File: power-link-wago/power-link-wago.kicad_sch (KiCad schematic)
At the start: 12 parts, among them J101 NE8FAV, J102 NE8FAV, J103 WAGO 2601-1101, J104 WAGO 2601-1101, J105 WAGO 2601-1101, J106 WAGO 2601-1101

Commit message: Rename power-poe -> power-link-wago
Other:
- title: V2 Power PoE -> V2 Power Link WAGO
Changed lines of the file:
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@@
 	(paper "A4")
 	(title_block
-		(title "V2 Power PoE")
+		(title "V2 Power Link WAGO")
 		(date "2026-01-12")
 		(rev "3")
@@
 		)
 		(instances
-			(project "power-poe"
+			(project "power-link-wago"
 				(path "/6c8448b4-b04d-47e1-934e-e40cbe27a7be"
 					(reference "#FLG0103")
@@
 		)
 		(instances
-			(project "power-poe"
+			(project "power-link-wago"
 				(path "/6c8448b4-b04d-47e1-934e-e40cbe27a7be"
 					(reference "J103")
@@
 		)
 		(instances
-			(project "power-poe"
+			(project "power-link-wago"
 				(path "/6c8448b4-b04d-47e1-934e-e40cbe27a7be"
 					(reference "ICON103")
@@
 		)
 		(instances
-			(project "power-poe"
+			(project "power-link-wago"
 				(path "/6c8448b4-b04d-47e1-934e-e40cbe27a7be"
 					(reference "J106")
@@
 		)
 		(instances
-			(project "power-poe"
+			(project "power-link-wago"
 				(path "/6c8448b4-b04d-47e1-934e-e40cbe27a7be"
 					(reference "#PWR0108")
@@
 		)
 		(instances
-			(project "power-poe"
+			(project "power-link-wago"
 				(path "/6c8448b4-b04d-47e1-934e-e40cbe27a7be"
 					(reference "#PWR0107")
@@
 		)
 		(instances
-			(project "power-poe"
+			(project "power-link-wago"
 				(path "/6c8448b4-b04d-47e1-934e-e40cbe27a7be"
 					(reference "#PWR0110")
@@
 		)
 		(instances
-			(project "power-poe"
+			(project "power-link-wago"
 				(path "/6c8448b4-b04d-47e1-934e-e40cbe27a7be"
 					(reference "J105")
@@
 		)
 		(instances
-			(project "power-poe"
+			(project "power-link-wago"
 				(path "/6c8448b4-b04d-47e1-934e-e40cbe27a7be"
 					(reference "#PWR0111")
@@
 		)
 		(instances
-			(project "power-poe"
+			(project "power-link-wago"
 				(path "/6c8448b4-b04d-47e1-934e-e40cbe27a7be"
 					(reference "H102")

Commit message: Fix WAGOs
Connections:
- net +24V renamed +VLINK
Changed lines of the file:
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@@
 			)
 		)
-		(property "Description" "Power symbol creates a global label with name \"Earth\""
+		(property "Description" "Power symbol creates a global label with name \"Shield\""
 			(at 119.38 103.632 0)
 			(effects
@@
 	(symbol
 		(lib_id "V2_power:PWR_FLAG")
-		(at 149.86 55.88 90)
+		(at 149.86 54.61 90)
 		(unit 1)
 		(exclude_from_sim no)
@@
 		(dnp no)
 		(property "Reference" "#FLG0103"
-			(at 147.955 55.88 0)
+			(at 147.955 54.61 0)
 			(effects
 				(font
@@
 		)
 		(property "Value" "PWR_FLAG"
-			(at 138.938 55.88 90)
+			(at 138.938 54.61 90)
 			(effects
 				(font
@@
 		)
 		(property "Footprint" ""
-			(at 149.86 55.88 0)
-			(effects
-				(font
-					(size 1.27 1.27)
-				)
-				(hide yes)
-			)
-		)
-		(property "Datasheet" ""
-			(at 149.86 55.88 0)
+			(at 149.86 54.61 0)
+			(effects
+				(font
+					(size 1.27 1.27)
+				)
+				(hide yes)
+			)
+		)
+		(property "Datasheet" ""
+			(at 149.86 54.61 0)
 			(effects
 				(font
@@
 		)
 		(property "Description" "Special symbol for telling ERC where power comes from"
-			(at 167.132 55.88 0)
+			(at 167.132 54.61 0)
 			(effects
 				(font
@@
 	)
 	(symbol
-		(lib_id "V2_power:+24V")
+		(lib_id "V2_power:+VLINK")
 		(at 149.86 44.45 270)
 		(unit 1)
@@
 			)
 		)
-		(property "Value" "+24V"
+		(property "Value" "+VLINK"
 			(at 156.972 44.45 90)
 			(effects
@@
 			)
 		)
-		(property "Description" "Power symbol creates a global label with name \"+24V\""
+		(property "Description" "Power symbol creates a global label with name \"+VLINK\""
 			(at 135.128 44.45 0)
 			(effects
@@
 	)
 	(symbol
-		(lib_id "V2_power:+24V")
+		(lib_id "V2_power:+VLINK")
 		(at 158.75 135.89 0)
 		(unit 1)
@@
 			)
 		)
-		(property "Value" "+24V"
+		(property "Value" "+VLINK"
 			(at 156.464 130.81 0)
 			(effects
@@
 			)
 		)
-		(property "Description" "Power symbol creates a global label with name \"+24V\""
+		(property "Description" "Power symbol creates a global label with name \"+VLINK\""
 			(at 158.75 150.622 0)
 			(effects
@@
 			)
 		)
-		(property "Description" "Power symbol creates a global label with name \"Earth\""
+		(property "Description" "Power symbol creates a global label with name \"Shield\""
 			(at 165.1 103.632 0)
 			(effects
@@
 	)
 	(symbol
-		(lib_id "V2_power:+24V")
+		(lib_id "V2_power:+VLINK")
 		(at 129.54 77.47 270)
 		(unit 1)
@@
 			)
 		)
-		(property "Value" "+24V"
+		(property "Value" "+VLINK"
 			(at 133.35 77.4699 90)
 			(effects
@@
 			)
 		)
-		(property "Description" "Power symbol creates a global label with name \"+24V\""
+		(property "Description" "Power symbol creates a global label with name \"+VLINK\""
 			(at 114.808 77.47 0)
 			(effects
@@
 	)
 	(symbol
-		(lib_id "V2_power:+24V")
+		(lib_id "V2_power:+VLINK")
 		(at 175.26 77.47 270)
 		(unit 1)
@@
 			)
 		)
-		(property "Value" "+24V"
+		(property "Value" "+VLINK"
 			(at 179.07 77.4699 90)
 			(effects
@@
 			)
 		)
-		(property "Description" "Power symbol creates a global label with name \"+24V\""
+		(property "Description" "Power symbol creates a global label with name \"+VLINK\""
 			(at 160.528 77.47 0)
 			(effects
@@
 	(symbol
 		(lib_id "V2_power:Shield")
-		(at 149.86 55.88 90)
+		(at 149.86 54.61 90)
 		(unit 1)
 		(exclude_from_sim no)
@@
 		(fields_autoplaced yes)
 		(property "Reference" "#PWR0111"
-			(at 157.48 55.88 0)
+			(at 157.48 54.61 0)
 			(effects
 				(font
@@
 		)
 		(property "Value" "Shield"
-			(at 153.67 55.8799 90)
+			(at 153.67 54.6099 90)
 			(effects
 				(font
@@
 		)
 		(property "Footprint" ""
-			(at 149.86 55.88 0)
-			(effects
-				(font
-					(size 1.27 1.27)
-				)
-				(hide yes)
-			)
-		)
-		(property "Datasheet" ""
-			(at 149.86 55.88 0)
-			(effects
-				(font
-					(size 1.27 1.27)
-				)
-				(hide yes)
-			)
-		)
-		(property "Description" "Power symbol creates a global label with name \"Earth\""
-			(at 160.782 55.88 0)
-			(effects
-				(font
+			(at 149.86 54.61 0)
+			(effects
+				(font
+					(size 1.27 1.27)
+				)
+				(hide yes)
+			)
+		)
+		(property "Datasheet" ""
+			(at 149.86 54.61 0)
+			(effects
+				(font
+					(size 1.27 1.27)
+				)
+				(hide yes)
+			)
+		)
+		(property "Description" "Power symbol creates a global label with name \"Shield\""
+			(at 160.782 54.61 0)
+			(effects
+				(font

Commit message: Use date as revision
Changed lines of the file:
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@@
 	(title_block
 		(title "V2 Power Link WAGO")
-		(date "2026-01-12")
-		(rev "3")
+		(date "2026-02-10")
+		(rev "2026-01-12")
 		(company "Versio Duo")
 	)
@@
 			)
 		)
-		(property "Description" "Power symbol creates a global label with name \"Shield\""
+		(property "Description" ""
 			(at 119.38 103.632 0)
 			(effects
@@
 			)
 		)
-		(property "Description" "Power symbol creates a global label with name \"GND\" , ground"
+		(property "Description" ""
 			(at 160.274 49.784 0)
 			(effects
@@
 			)
 		)
-		(property "Description" "Power symbol creates a global label with name \"+VLINK\""
+		(property "Description" "Power Over CAT Cable"
 			(at 135.128 44.45 0)
 			(effects
@@
 			)
 		)
-		(property "Description" "Power symbol creates a global label with name \"GND\" , ground"
+		(property "Description" ""
 			(at 122.936 153.924 0)
 			(effects
@@
 			)
 		)
-		(property "Description" "Power symbol creates a global label with name \"+VLINK\""
+		(property "Description" "Power Over CAT Cable"
 			(at 158.75 150.622 0)
 			(effects
@@
 			)
 		)
-		(property "Description" "Power symbol creates a global label with name \"Shield\""
+		(property "Description" ""
 			(at 165.1 103.632 0)
 			(effects
@@
 			)
 		)
-		(property "Description" "Power symbol creates a global label with name \"+VLINK\""
+		(property "Description" "Power Over CAT Cable"
 			(at 114.808 77.47 0)
 			(effects
@@
 			)
 		)
-		(property "Description" "Power symbol creates a global label with name \"GND\" , ground"
+		(property "Description" ""
 			(at 185.674 70.104 0)
 			(effects
@@
 			)
 		)
-		(property "Description" "Power symbol creates a global label with name \"GND\" , ground"
+		(property "Description" ""
 			(at 139.954 70.104 0)
 			(effects
@@
 			)
 		)
-		(property "Description" "Power symbol creates a global label with name \"+VLINK\""
+		(property "Description" "Power Over CAT Cable"
 			(at 160.528 77.47 0)
 			(effects
@@
 			)
 		)
-		(property "Description" "Power symbol creates a global label with name \"Shield\""
+		(property "Description" ""
 			(at 160.782 54.61 0)
 			(effects
@@
 	)
 	(embedded_fonts no)
+	(embedded_files
+		(file
+			(name "V2_A4.kicad_wks")
+			(type worksheet)
+			(data |KLUv/WBhBk0QALbYTiEQtRsmZc5q276ayLS71D6kxbkmoTeIJM7lAHtEAMAAxQFGAD8ARQCbvIHa
+				a/wrVHSazXnPhvzar1BNtH1kxRf5EwCAQPh5F+e0kJq0nmtfKDvj37Jf3xQUlFKqztoXWzE7iAAI
+				iJ6Q5m2d9RAC9jcPPWe/GXf/9ewpPR3+uPbv7bdzvr37wXlr2X8dBHFXu7Z3HUG7Kvrz9qKU7eB2
+				v/MM4n/Mhfg5G5sn7WsDTS2mA1WyssZDsy4YdpEGzfD8Ny+85JzH7H+961FjX/x0qtq0MdaqJ8dx
+				k1KAwF+soV3VFnEoqewX+XNfTaqqPatRlLsbgcKhzs5+29sEzSaWRPZ4txDEjpmZNCoSiiMhaUwy
+				y4Jg3oe5pmhPRSS7MtJAerbfnYNNgaEkuCg6oVzYhbEsF1vRgtxS55zTIVig4URjFFJTI1qYFNIB
+				YESmRusYYvaiF0uSUdhu1Q2lFiOgdmN7VvaH2oWyw9MQXRuZtQQQoIsxFn2ldtnpQiUNa0HvDQCK
+				f/XTisCgEJQEXe/if4EJsakkqj8BMmGAU+ZM/AG8LSEJMfgkOKfSKPhw4rD3ZHfmNZYNfDMigEPJ
+				EBoIDghtm1kJ8BAQ8xyGdkOuFQy33sishFt8DZNX4uNRXJZ5hBy746RJaNtgbfyB613d0dov6Cdg
+				iUQT9BXkf9EiYDuODpB6gKkC|
+			)
+			(checksum "0A61268C685EAF945CA2EA8187370BD3")
+		)
+	)
 )

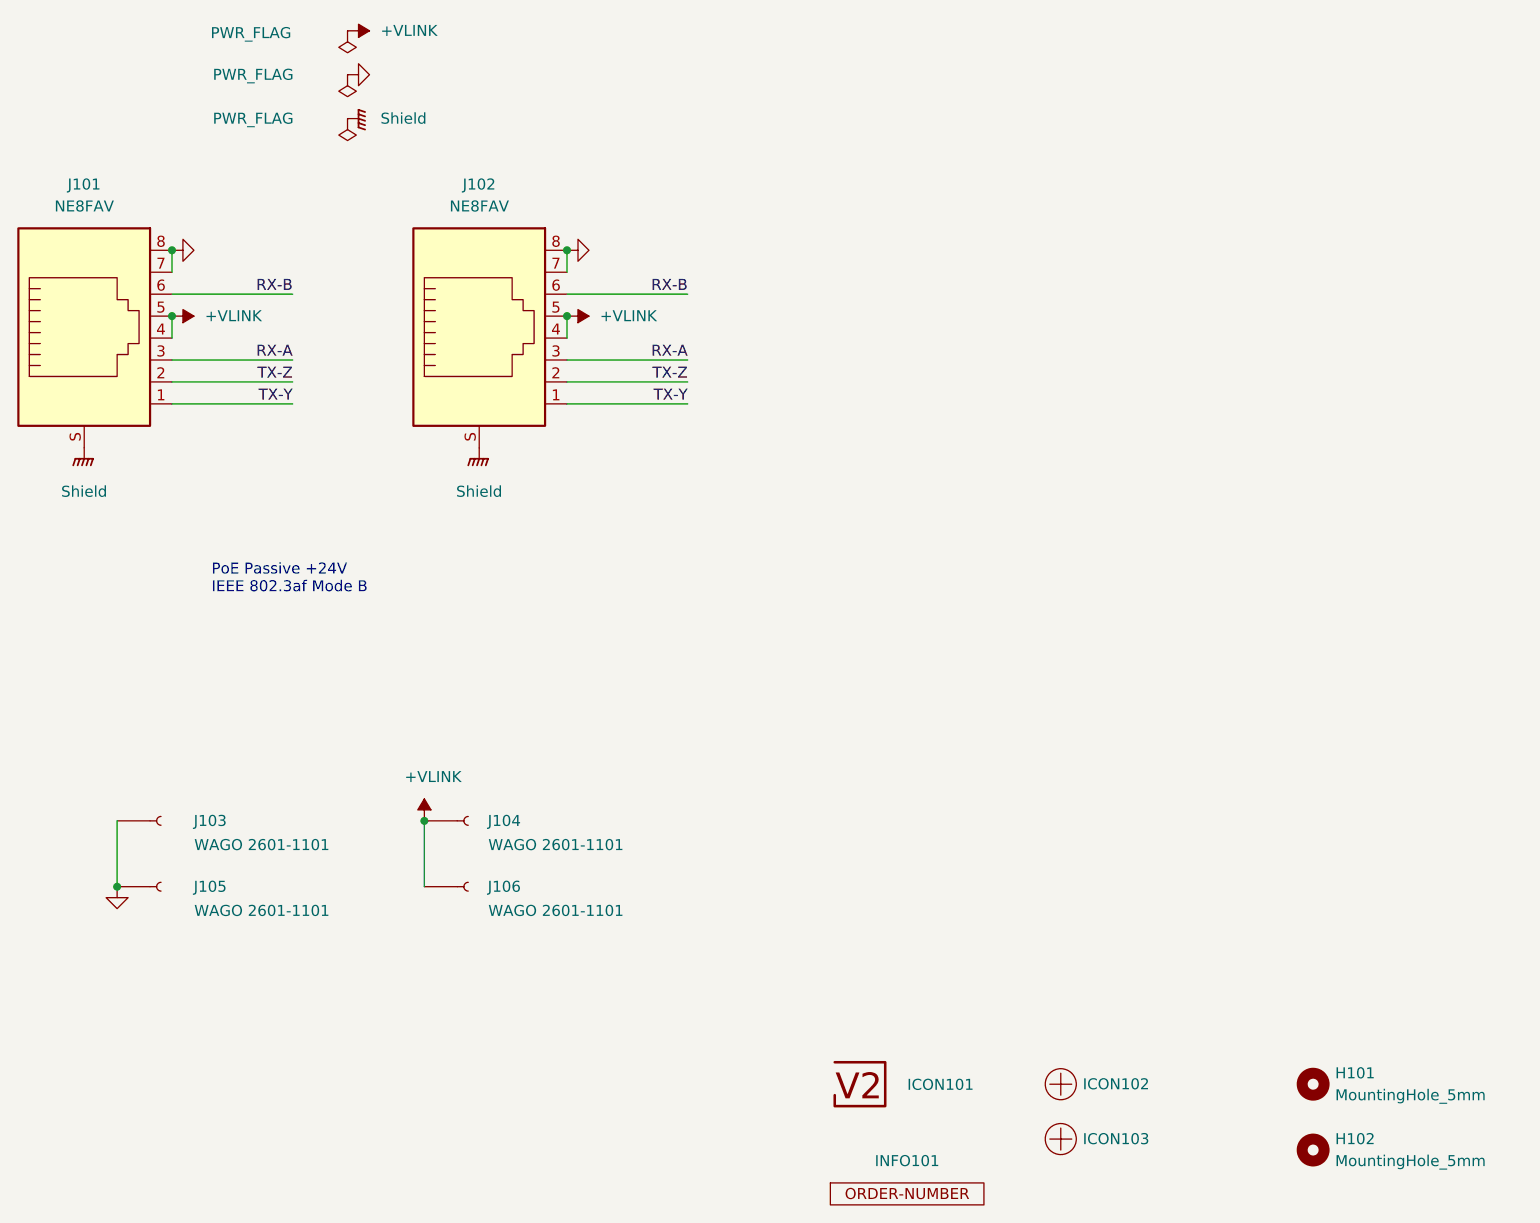
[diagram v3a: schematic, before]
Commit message: Replace Order_Number
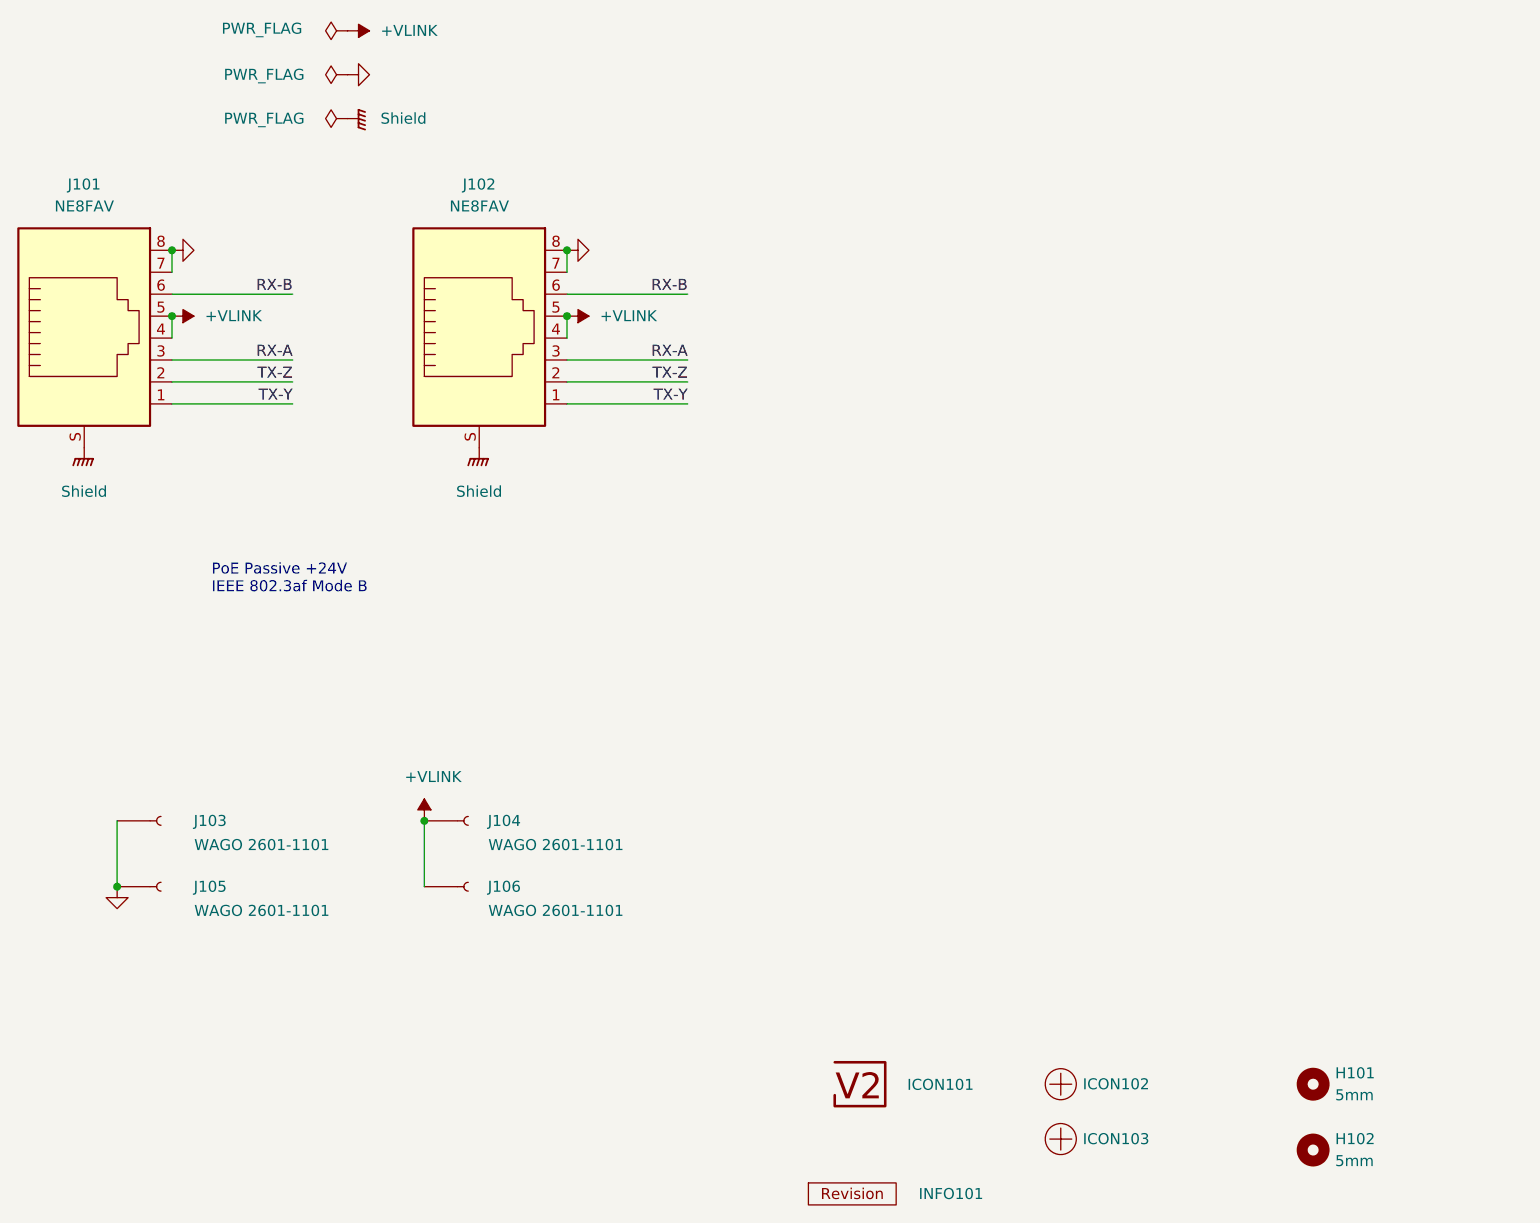
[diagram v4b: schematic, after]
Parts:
- H101, H102: value MountingHole_5mm -> 5mm
- INFO101: value Order_Number -> ~; footprint V2_Production:Order_Number -> V2_Production:Revision; symbol V2_Production:Order_Number -> V2_Production:Revision
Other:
- moved on the sheet: INFO101
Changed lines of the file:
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@@
 	(symbol
 		(lib_id "V2_power:PWR_FLAG")
-		(at 149.86 54.61 90)
+		(at 149.86 54.61 0)
 		(unit 1)
 		(exclude_from_sim no)
@@
 		(dnp no)
 		(property "Reference" "#FLG0103"
-			(at 147.955 54.61 0)
+			(at 149.86 52.705 0)
 			(effects
 				(font
@@
 		)
 		(property "Value" "PWR_FLAG"
-			(at 138.938 54.61 90)
+			(at 140.208 54.61 0)
 			(effects
 				(font
@@
 		)
 		(property "Description" "Special symbol for telling ERC where power comes from"
-			(at 167.132 54.61 0)
+			(at 149.86 71.882 0)
 			(effects
 				(font
@@
 			)
 		)
-		(property "Sim.Enable" "0"
-			(at 209.55 166.37 0)
-			(effects
-				(font
-					(size 1.27 1.27)
-				)
-				(hide yes)
-			)
-		)
 		(instances
 			(project ""
@@
 	(symbol
 		(lib_id "V2_power:PWR_FLAG")
-		(at 149.86 49.53 90)
+		(at 149.86 49.53 0)
 		(unit 1)
 		(exclude_from_sim no)
@@
 		(dnp no)
 		(property "Reference" "#FLG0102"
-			(at 147.955 49.53 0)
+			(at 149.86 47.625 0)
 			(effects
 				(font
@@
 		)
 		(property "Value" "PWR_FLAG"
-			(at 138.938 49.53 90)
+			(at 140.208 49.53 0)
 			(effects
 				(font
@@
 		)
 		(property "Description" "Special symbol for telling ERC where power comes from"
-			(at 167.132 49.53 0)
+			(at 149.86 66.802 0)
 			(effects
 				(font
@@
 	)
 	(symbol
-		(lib_id "V2_Production:Order_Number")
-		(at 214.63 179.07 0)
+		(lib_id "V2_Production:Revision")
+		(at 208.28 179.07 0)
 		(unit 1)
 		(exclude_from_sim no)
@@
 		(dnp no)
 		(property "Reference" "INFO101"
-			(at 214.63 175.26 0)
-			(effects
-				(font
-					(size 1.27 1.27)
-				)
-			)
-		)
-		(property "Value" "Order_Number"
-			(at 214.63 181.61 0)
-			(effects
-				(font
-					(size 1.27 1.27)
-				)
-				(hide yes)
-			)
-		)
-		(property "Footprint" "V2_Production:Order_Number"
-			(at 214.63 184.15 0)
-			(effects
-				(font
-					(size 1.27 1.27)
-				)
-				(hide yes)
-			)
-		)
-		(property "Datasheet" ""
-			(at 214.63 179.07 0)
+			(at 219.71 179.07 0)
+			(effects
+				(font
+					(size 1.27 1.27)
+				)
+			)
+		)
+		(property "Value" "~"
+			(at 208.28 181.61 0)
+			(effects
+				(font
+					(size 1.27 1.27)
+				)
+				(hide yes)
+			)
+		)
+		(property "Footprint" "V2_Production:Revision"
+			(at 208.28 184.15 0)
+			(effects
+				(font
+					(size 1.27 1.27)
+				)
+				(hide yes)
+			)
+		)
+		(property "Datasheet" ""
+			(at 208.28 179.07 0)
 			(effects
 				(font
@@
 		)
 		(property "Description" ""
-			(at 214.63 179.07 0)
+			(at 208.28 179.07 0)
 			(effects
 				(font
@@
 			)
 		)
-		(property "Value" "MountingHole_5mm"
+		(property "Value" "5mm"
 			(at 264.16 167.6399 0)
 			(effects
@@
 			)
 		)
-		(property "Sim.Enable" "0"
-			(at 261.62 166.37 0)
-			(effects
-				(font
-					(size 1.27 1.27)
-				)
-				(hide yes)
-			)
-		)
 		(instances
 			(project ""
@@
 	(symbol
 		(lib_id "V2_power:PWR_FLAG")
-		(at 149.86 44.45 90)
+		(at 149.86 44.45 0)
 		(unit 1)
 		(exclude_from_sim no)
@@
 		(dnp no)
 		(property "Reference" "#FLG0101"
-			(at 147.955 44.45 0)
+			(at 149.86 42.545 0)
 			(effects
 				(font
@@
 		)
 		(property "Value" "PWR_FLAG"
-			(at 138.684 44.704 90)
+			(at 139.954 44.196 0)
 			(effects
 				(font
@@
 		)
 		(property "Description" "Special symbol for telling ERC where power comes from"
-			(at 167.132 44.45 0)
+			(at 149.86 61.722 0)
 			(effects
 				(font
@@
 			)
 		)
-		(property "Value" "MountingHole_5mm"
+		(property "Value" "5mm"
 			(at 264.16 175.2599 0)
 			(effects
@@
 			(at 261.62 173.99 0)
 			(effects
-				(font
-					(size 1.27 1.27)
-				)
-				(hide yes)
-			)
-		)
-		(property "Sim.Enable" "0"
-			(at 261.62 173.99 0)
-			(effects

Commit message: Refresh
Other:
- note added: "PoE Passive +28V IEEE 802.3af Mode B"
- note removed: "PoE Passive +24V IEEE 802.3af Mode B"
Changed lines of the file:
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@@
 		(company "Versio Duo")
 	)
-	(text "PoE Passive +24V\nIEEE 802.3af Mode B"
+	(text "PoE Passive +28V\nIEEE 802.3af Mode B"
 		(exclude_from_sim no)
 		(at 134.112 107.95 0)
@@
 		(at 232.41 172.72 0)
 		(unit 1)
-		(exclude_from_sim no)
+		(exclude_from_sim yes)
 		(in_bom no)
 		(on_board yes)
@@
 			)
 		)
-		(property "Sim.Enable" "0"
-			(at 232.41 172.72 0)
-			(effects
-				(font
-					(size 1.27 1.27)
-				)
-				(hide yes)
-			)
-		)
 		(instances
 			(project "power-link-wago"
@@
 		(at 232.41 166.37 0)
 		(unit 1)
-		(exclude_from_sim no)
+		(exclude_from_sim yes)
 		(in_bom no)
 		(on_board yes)
@@
 			(at 232.41 166.37 0)
 			(effects
-				(font
-					(size 1.27 1.27)
-				)
-				(hide yes)
-			)
-		)
-		(property "Sim.Enable" "0"
-			(at 232.41 166.37 0)
-			(effects

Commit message: Export stencil
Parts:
- INFO101: value ~ -> (none)
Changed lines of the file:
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@@
 	(title_block
 		(title "V2 Power Link WAGO")
-		(date "2026-02-10")
+		(date "2026-02-25")
 		(rev "2026-01-12")
 		(company "Versio Duo")
@@
 		(at 232.41 172.72 0)
 		(unit 1)
-		(exclude_from_sim yes)
+		(exclude_from_sim no)
 		(in_bom no)
 		(on_board yes)
@@
 			)
 		)
+		(property "Sim.Enable" "0"
+			(at 232.41 172.72 0)
+			(effects
+				(font
+					(size 1.27 1.27)
+				)
+				(hide yes)
+			)
+		)
 		(instances
 			(project "power-link-wago"
@@
 			)
 		)
-		(property "Value" "~"
+		(property "Value" ""
 			(at 208.28 181.61 0)
 			(effects
@@
 		(at 232.41 166.37 0)
 		(unit 1)
-		(exclude_from_sim yes)
+		(exclude_from_sim no)
 		(in_bom no)
 		(on_board yes)
@@
 			(at 232.41 166.37 0)
 			(effects
+				(font
+					(size 1.27 1.27)
+				)
+				(hide yes)
+			)
+		)
+		(property "Sim.Enable" "0"
+			(at 232.41 166.37 0)
+			(effects
